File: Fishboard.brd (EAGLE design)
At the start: 47.9 x 61 mm, 23 parts, among them J3 B1, J4 B2, J5 B3, J7 B4, Q1 TIP120, Q2 TIP120, Q3 TIP120

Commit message: Reorganized schematics
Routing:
- added copper zone on layer 1, net N$7
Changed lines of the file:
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@@
 <wire x1="30.48" y1="27.94" x2="30.48" y2="26.67" width="1.27" layer="1"/>
+</signal>
+<signal name="N$7">
+<polygon width="0.4064" layer="1">
+<vertex x="1.27" y="20.32"/>
+<vertex x="0" y="20.32"/>
+<vertex x="0" y="0"/>
+<vertex x="48.26" y="0"/>
+<vertex x="48.26" y="15.24"/>
+<vertex x="46.99" y="15.24"/>
+<vertex x="45.72" y="13.97"/>
+<vertex x="43.18" y="13.97"/>
+<vertex x="41.91" y="15.24"/>
+<vertex x="41.91" y="16.51"/>
+<vertex x="40.64" y="17.78"/>
+<vertex x="2.54" y="17.78"/>
+<vertex x="1.27" y="19.05"/>
+</polygon>
 </signal>
 </signals>

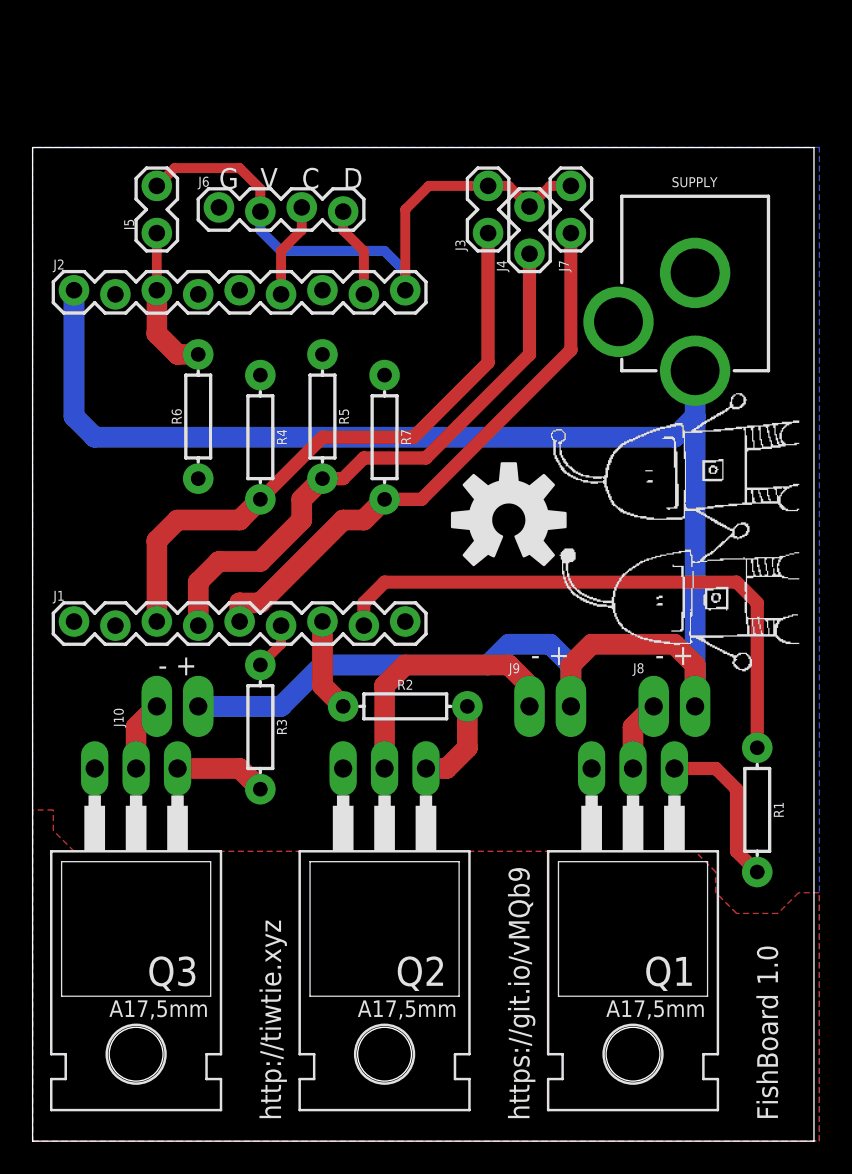
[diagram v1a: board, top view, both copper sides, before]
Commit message: Switched the TIP120 with a logic level MOSFET (FQP30N06L). The current limiting resistors have been replaced with pulldowns.
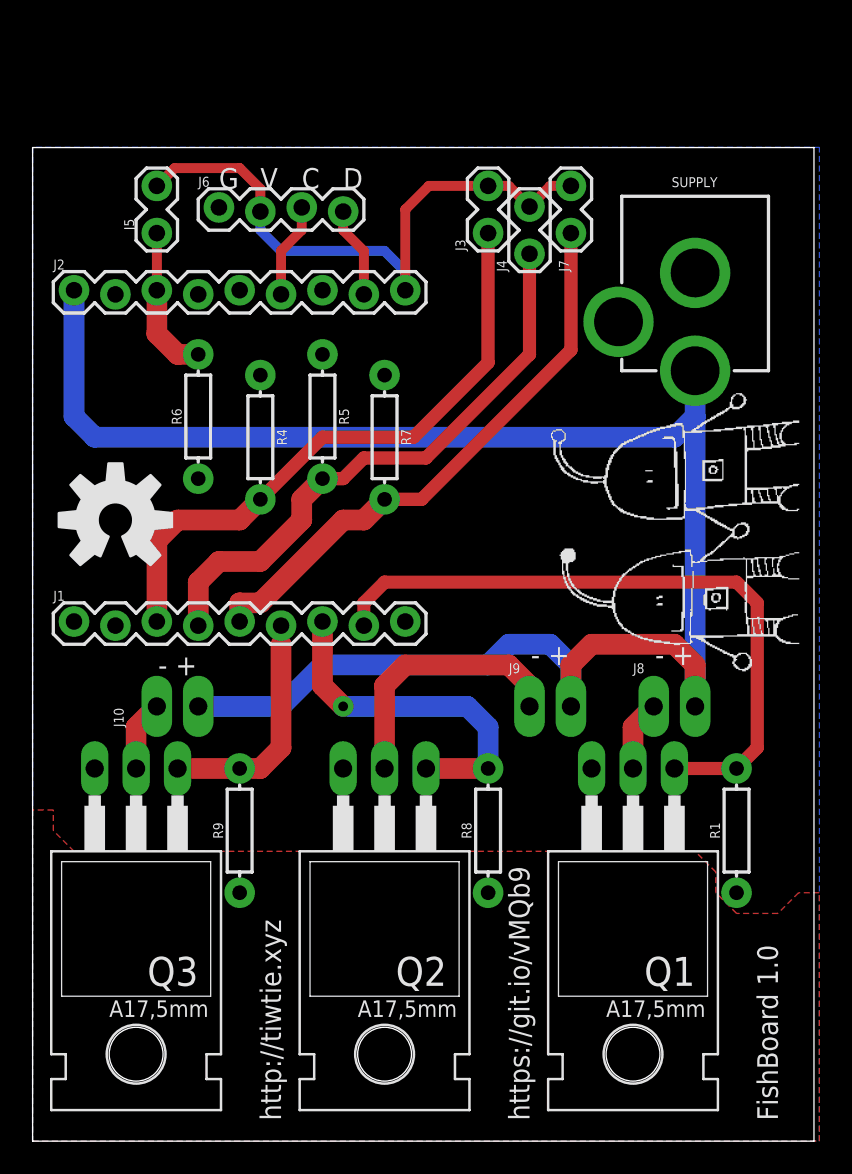
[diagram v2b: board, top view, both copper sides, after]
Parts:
- removed R2, R3: 820R, SparkFun-Resistors:AXIAL-0.3
- added R8, R9: 100k, SparkFun-Resistors:AXIAL-0.3
- Q1, Q2, Q3: value TIP120 -> FQP30N06L
- R1: value 820R -> 100k
- moved U$2 24.1 mm to (5.08, 38.1)
- moved R1 1.80 mm to (43.2, 19.1), turned to 90 degrees
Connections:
- removed net N$2: Q1.B, R1.P$2
- removed net N$3: Q2.B, R2.P$2
- removed net N$4: Q3.B, R3.P$2
- net DEV1_EN: now also Q1.B, R1.P$2; no longer R1.P$1
- net DEV2_EN: now also Q2.B, R8.P$2; no longer R2.P$1
- net DEV3_EN: now also Q3.B, R9.P$2; no longer R3.P$1
- net GND: now also R1.P$1, R8.P$1, R9.P$1
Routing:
- net DEV2_EN: track 5.73 -> 21.5 mm, vias 0 -> 1
- net DEV3_EN: track 2.94 -> 14.4 mm
- net N$2: track 9.94 -> 0.00 mm
- net N$3: track 5.61 -> 0.00 mm
- net N$4: track 5.61 -> 0.00 mm
- net DEV1_EN: track 35.5 -> 41.1 mm
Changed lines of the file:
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@@
 <element name="J1" library="SparkFun-Connectors" package="1X09_LOCK" value="" x="2.54" y="31.75"/>
 <element name="J2" library="SparkFun-Connectors" package="1X09_LOCK" value="" x="2.54" y="52.07"/>
-<element name="Q1" library="transistor-power" package="TO220AH" value="TIP120" x="36.83" y="16.51" rot="R180"/>
-<element name="Q2" library="transistor-power" package="TO220AH" value="TIP120" x="21.59" y="16.51" rot="R180"/>
-<element name="Q3" library="transistor-power" package="TO220AH" value="TIP120" x="6.35" y="16.51" rot="R180"/>
-<element name="R1" library="SparkFun-Resistors" package="AXIAL-0.3" value="820R" x="44.45" y="20.32" rot="R270">
-<attribute name="PROD_ID" value="RES-08380" x="44.45" y="20.32" size="1.778" layer="27" rot="R270" display="off"/>
+<element name="Q1" library="transistor-power" package="TO220AH" value="FQP30N06L" x="36.83" y="16.51" smashed="yes" rot="R180">
+<attribute name="NAME" x="40.64" y="11.303" size="1.778" layer="25" ratio="10" rot="R180"/>
+<attribute name="VALUE" x="40.767" y="13.97" size="1.016" layer="27" font="vector" ratio="10" rot="R180"/>
 </element>
-<element name="R2" library="SparkFun-Resistors" package="AXIAL-0.3" value="820R" x="22.86" y="26.67">
-<attribute name="PROD_ID" value="RES-08380" x="22.86" y="26.67" size="1.778" layer="27" display="off"/>
+<element name="Q2" library="transistor-power" package="TO220AH" value="FQP30N06L" x="21.59" y="16.51" smashed="yes" rot="R180">
+<attribute name="NAME" x="25.4" y="11.303" size="1.778" layer="25" ratio="10" rot="R180"/>
+<attribute name="VALUE" x="25.527" y="13.97" size="1.016" layer="27" font="vector" ratio="10" rot="R180"/>
 </element>
-<element name="R3" library="SparkFun-Resistors" package="AXIAL-0.3" value="820R" x="13.97" y="25.4" rot="R270">
-<attribute name="PROD_ID" value="RES-08380" x="13.97" y="25.4" size="1.778" layer="27" rot="R270" display="off"/>
+<element name="Q3" library="transistor-power" package="TO220AH" value="FQP30N06L" x="6.35" y="16.51" smashed="yes" rot="R180">
+<attribute name="NAME" x="10.16" y="11.303" size="1.778" layer="25" ratio="10" rot="R180"/>
+<attribute name="VALUE" x="10.287" y="13.97" size="1.016" layer="27" font="vector" ratio="10" rot="R180"/>
 </element>
 <element name="SUPPLY" library="SparkFun-Connectors" package="POWER_JACK_PTH" value="POWER_JACK" x="40.64" y="60.96" rot="R180">
@@
 </element>
 <element name="U$1" library="tiwtie" package="TIWTIE_LOGO" value="" x="46.99" y="27.94" rot="R90"/>
-<element name="U$2" library="SparkFun-Aesthetics" package="OSHW-LOGO-L" value="" x="29.21" y="38.1"/>
+<element name="U$2" library="SparkFun-Aesthetics" package="OSHW-LOGO-L" value="" x="5.08" y="38.1"/>
 <element name="J8" library="SparkFun-Connectors" package="1X02_LONGPADS" value="" x="38.1" y="26.67"/>
 <element name="J9" library="SparkFun-Connectors" package="1X02_LONGPADS" value="" x="30.48" y="26.67"/>
@@
 <attribute name="NAME" x="5.588" y="25.4" size="0.6096" layer="25" font="vector" ratio="20" rot="R90"/>
 <attribute name="VALUE" x="6.223" y="24.003" size="0.6096" layer="27" font="vector" ratio="20"/>
+</element>
+<element name="R1" library="SparkFun-Resistors" package="AXIAL-0.3" value="100k" x="43.18" y="19.05" smashed="yes" rot="R90">
+<attribute name="PROD_ID" value="RES-10686" x="43.18" y="19.05" size="1.778" layer="27" rot="R90" display="off"/>
+<attribute name="NAME" x="42.164" y="19.05" size="0.6096" layer="25" font="vector" ratio="20" rot="R90" align="bottom-center"/>
+<attribute name="VALUE" x="42.926" y="20.32" size="0.6096" layer="27" font="vector" ratio="20" rot="R90" align="top-center"/>
+</element>
+<element name="R8" library="SparkFun-Resistors" package="AXIAL-0.3" value="100k" x="27.94" y="19.05" smashed="yes" rot="R90">
+<attribute name="PROD_ID" value="RES-10686" x="27.94" y="19.05" size="1.778" layer="27" rot="R90" display="off"/>
+<attribute name="NAME" x="26.924" y="19.05" size="0.6096" layer="25" font="vector" ratio="20" rot="R90" align="bottom-center"/>
+<attribute name="VALUE" x="27.686" y="20.32" size="0.6096" layer="27" font="vector" ratio="20" rot="R90" align="top-center"/>
+</element>
+<element name="R9" library="SparkFun-Resistors" package="AXIAL-0.3" value="100k" x="12.7" y="19.05" smashed="yes" rot="R90">
+<attribute name="PROD_ID" value="RES-10686" x="12.7" y="19.05" size="1.778" layer="27" rot="R90" display="off"/>
+<attribute name="NAME" x="11.684" y="19.05" size="0.6096" layer="25" font="vector" ratio="20" rot="R90" align="bottom-center"/>
+<attribute name="VALUE" x="12.446" y="20.32" size="0.6096" layer="27" font="vector" ratio="20" rot="R90" align="top-center"/>
 </element>
 </elements>
@@
 <contactref element="R7" pad="P$1"/>
 <contactref element="J6" pad="1"/>
+<contactref element="R1" pad="P$1"/>
+<contactref element="R8" pad="P$1"/>
+<contactref element="R9" pad="P$1"/>
 </signal>
 <signal name="VCC12">
@@
 <wire x1="36.83" y1="25.4" x2="36.83" y2="22.86" width="1.27" layer="1"/>
 </signal>
-<signal name="N$2">
-<contactref element="Q1" pad="B"/>
-<contactref element="R1" pad="P$2"/>
-<wire x1="39.37" y1="22.86" x2="41.91" y2="22.86" width="0.8128" layer="1"/>
-<wire x1="41.91" y1="22.86" x2="43.18" y2="21.59" width="0.8128" layer="1"/>
-<wire x1="43.18" y1="21.59" x2="43.18" y2="17.78" width="0.8128" layer="1"/>
-<wire x1="43.18" y1="17.78" x2="44.45" y2="16.51" width="0.8128" layer="1"/>
-</signal>
-<signal name="N$3">
-<contactref element="Q2" pad="B"/>
-<contactref element="R2" pad="P$2"/>
-<wire x1="26.67" y1="26.67" x2="26.67" y2="24.13" width="1.27" layer="1"/>
-<wire x1="26.67" y1="24.13" x2="25.4" y2="22.86" width="1.27" layer="1"/>
-<wire x1="25.4" y1="22.86" x2="24.13" y2="22.86" width="1.27" layer="1"/>
-</signal>
-<signal name="N$4">
-<contactref element="Q3" pad="B"/>
-<contactref element="R3" pad="P$2"/>
-<wire x1="8.89" y1="22.86" x2="12.7" y2="22.86" width="1.27" layer="1"/>
-<wire x1="12.7" y1="22.86" x2="13.97" y2="21.59" width="1.27" layer="1"/>
-</signal>
 <signal name="DEV1_EN">
-<contactref element="R1" pad="P$1"/>
 <contactref element="J1" pad="8"/>
-<wire x1="44.45" y1="33.02" x2="44.45" y2="24.13" width="0.8128" layer="1"/>
 <wire x1="20.32" y1="31.623" x2="20.32" y2="33.02" width="0.8128" layer="1"/>
 <wire x1="20.32" y1="33.02" x2="21.59" y2="34.29" width="0.8128" layer="1"/>
 <wire x1="21.59" y1="34.29" x2="43.18" y2="34.29" width="0.8128" layer="1"/>
 <wire x1="43.18" y1="34.29" x2="44.45" y2="33.02" width="0.8128" layer="1"/>
+<contactref element="R1" pad="P$2"/>
+<contactref element="Q1" pad="B"/>
+<wire x1="44.45" y1="33.02" x2="44.45" y2="24.13" width="0.8128" layer="1"/>
+<wire x1="44.45" y1="24.13" x2="43.18" y2="22.86" width="0.8128" layer="1"/>
+<wire x1="39.37" y1="22.86" x2="43.18" y2="22.86" width="0.8128" layer="1"/>
 </signal>
 <signal name="DEV2_EN">
-<contactref element="R2" pad="P$1"/>
 <contactref element="J1" pad="7"/>
 <wire x1="17.78" y1="31.877" x2="17.78" y2="27.94" width="1.27" layer="1"/>
+<contactref element="R8" pad="P$2"/>
+<contactref element="Q2" pad="B"/>
+<wire x1="24.13" y1="22.86" x2="27.94" y2="22.86" width="1.27" layer="1"/>
 <wire x1="17.78" y1="27.94" x2="19.05" y2="26.67" width="1.27" layer="1"/>
+<via x="19.05" y="26.67" extent="1-16" drill="0.6" diameter="1.27"/>
+<wire x1="19.05" y1="26.67" x2="26.67" y2="26.67" width="1.27" layer="16"/>
+<wire x1="26.67" y1="26.67" x2="27.94" y2="25.4" width="1.27" layer="16"/>
+<wire x1="27.94" y1="25.4" x2="27.94" y2="22.86" width="1.27" layer="16"/>
 </signal>
 <signal name="DEV3_EN">
-<contactref element="R3" pad="P$1"/>
 <contactref element="J1" pad="6"/>
 <wire x1="15.24" y1="31.623" x2="15.24" y2="30.48" width="0.6096" layer="1"/>
-<wire x1="15.24" y1="30.48" x2="13.97" y2="29.21" width="0.6096" layer="1"/>
+<contactref element="R9" pad="P$2"/>
+<contactref element="Q3" pad="B"/>
+<wire x1="15.24" y1="30.48" x2="15.24" y2="24.13" width="1.27" layer="1"/>
+<wire x1="15.24" y1="24.13" x2="13.97" y2="22.86" width="1.27" layer="1"/>
+<wire x1="13.97" y1="22.86" x2="12.7" y2="22.86" width="1.27" layer="1"/>
+<wire x1="8.89" y1="22.86" x2="12.7" y2="22.86" width="1.27" layer="1"/>
 </signal>
 <signal name="D9">
